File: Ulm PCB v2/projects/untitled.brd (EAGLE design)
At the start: 39.4 x 53.1 mm, 26 parts, among them U1 FT232RLSSOP, U2 MCP73831, U3 SPX3819-3.3, X2 USB-SMD-NS

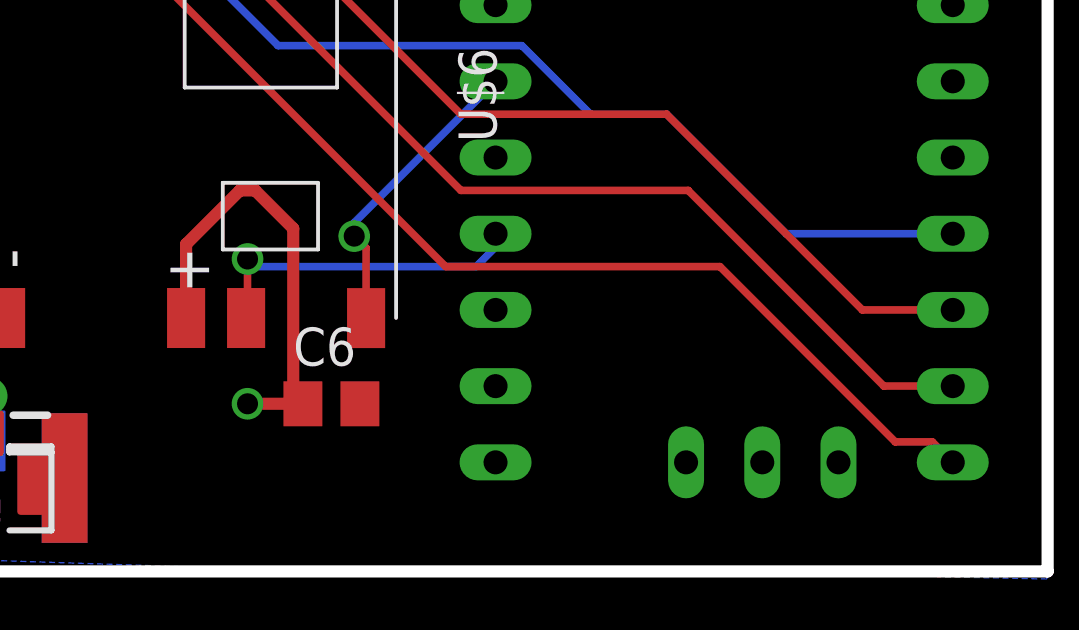
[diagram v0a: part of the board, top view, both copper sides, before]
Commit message: rerouted rmf power suppyl
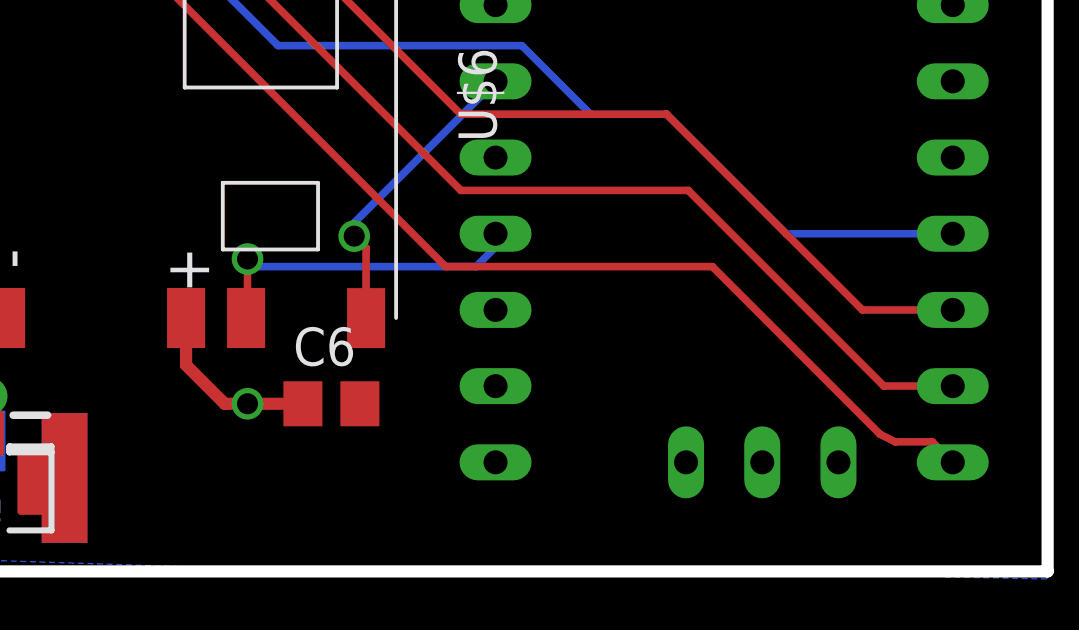
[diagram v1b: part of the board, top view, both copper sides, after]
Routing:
- net 3.3V: track 46.5 -> 37.9 mm
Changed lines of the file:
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@@
 <wire x1="0" y1="9.144" x2="39.37" y2="9.144" width="0.4064" layer="20"/>
 <wire x1="39.37" y1="9.144" x2="39.37" y2="62.23" width="0.4064" layer="20"/>
+<dimension x1="-0.508" y1="62.484" x2="-0.635" y2="9.144" x3="-7.555853125" y3="35.830628125" textsize="1.778" layer="1"/>
+<dimension x1="-0.508" y1="62.484" x2="39.4462" y2="62.4078" x3="19.482809375" y3="69.6344125" textsize="1.778" layer="1"/>
 </plain>
 <attributes>
@@
 <wire x1="27.178" y1="43.39936875" x2="27.3174625" y2="43.25990625" width="0.4064" layer="1"/>
 <wire x1="20.18615" y1="47.24329375" x2="20.828" y2="46.60144375" width="0.4064" layer="1"/>
-<wire x1="10.652" y1="17.5905" x2="10.652" y2="20.05" width="0.4064" layer="1"/>
-<wire x1="10.652" y1="20.05" x2="12.446" y2="21.844" width="0.4064" layer="1"/>
-<wire x1="12.446" y1="21.844" x2="12.954" y2="21.844" width="0.4064" layer="1"/>
-<wire x1="12.954" y1="21.844" x2="14.224" y2="20.574" width="0.4064" layer="1"/>
-<wire x1="14.224" y1="20.574" x2="14.224" y2="15.052" width="0.4064" layer="1"/>
 <wire x1="14.544" y1="14.732" x2="14.224" y2="15.052" width="0.4064" layer="1"/>
 <via x="12.7" y="14.732" extent="1-16" drill="0.7"/>
 <wire x1="12.7" y1="14.732" x2="14.544" y2="14.732" width="0.4064" layer="1"/>
 <wire x1="20.18615" y1="47.93765" x2="20.18615" y2="47.24329375" width="0.4064" layer="1"/>
+<wire x1="10.652" y1="17.5905" x2="10.652" y2="16.018" width="0.4064" layer="1"/>
+<wire x1="10.652" y1="16.018" x2="11.938" y2="14.732" width="0.4064" layer="1"/>
+<wire x1="11.938" y1="14.732" x2="12.7" y2="14.732" width="0.4064" layer="1"/>
 </signal>
 <signal name="TXLED">
@@
 <wire x1="8.652" y1="33.5905" x2="8.652" y2="29.956" width="0.254" layer="1"/>
 <wire x1="8.652" y1="29.956" x2="19.304" y2="19.304" width="0.254" layer="1"/>
-<wire x1="19.304" y1="19.304" x2="28.448" y2="19.304" width="0.254" layer="1"/>
-<wire x1="28.448" y1="19.304" x2="34.29" y2="13.462" width="0.254" layer="1"/>
 <wire x1="34.29" y1="13.462" x2="35.52536875" y2="13.462" width="0.254" layer="1"/>
 <wire x1="35.52536875" y1="13.462" x2="36.2074625" y2="12.77990625" width="0.254" layer="1"/>
+<wire x1="19.304" y1="19.304" x2="28.194" y2="19.304" width="0.254" layer="1"/>
+<wire x1="28.194" y1="19.304" x2="33.782" y2="13.716" width="0.254" layer="1"/>
+<wire x1="33.782" y1="13.716" x2="34.29" y2="13.462" width="0.254" layer="1"/>
 </signal>
 <signal name="LOL">

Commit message: rerouted arduino power suppyl
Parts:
- moved C7 2.54 mm to (28.4, 46.5)
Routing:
- net 3.3V: track 37.9 -> 34.0 mm
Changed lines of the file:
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@@
 </element>
 <element name="C6" library="rcl" package="C0805" value="100n" x="15.494" y="14.732"/>
-<element name="C7" library="rcl" package="C0805" value="100n" x="30.988" y="46.482"/>
+<element name="C7" library="rcl" package="C0805" value="100n" x="28.448" y="46.482"/>
 <element name="U$6" library="_c2h" package="RFM95" value="RFM95" x="9.652" y="23.368" rot="R270"/>
 <element name="C8" library="microbuilder" package="0805-NO" value="10µF" x="16.256" y="50.038" rot="R270"/>
@@
 </polygon>
 <wire x1="20.828" y1="46.60144375" x2="16.90025" y2="46.60144375" width="0.4064" layer="1"/>
-<wire x1="20.828" y1="46.60144375" x2="29.91855625" y2="46.60144375" width="0.4064" layer="1"/>
-<wire x1="29.91855625" y1="46.60144375" x2="30.038" y2="46.482" width="0.4064" layer="1"/>
-<wire x1="30.038" y1="46.482" x2="29.718" y2="46.482" width="0.4064" layer="1"/>
-<wire x1="29.718" y1="46.482" x2="27.178" y2="43.942" width="0.4064" layer="1"/>
-<wire x1="27.178" y1="43.942" x2="27.178" y2="43.39936875" width="0.4064" layer="1"/>
-<wire x1="27.178" y1="43.39936875" x2="27.3174625" y2="43.25990625" width="0.4064" layer="1"/>
 <wire x1="20.18615" y1="47.24329375" x2="20.828" y2="46.60144375" width="0.4064" layer="1"/>
 <wire x1="14.544" y1="14.732" x2="14.224" y2="15.052" width="0.4064" layer="1"/>
@@
 <wire x1="10.652" y1="16.018" x2="11.938" y2="14.732" width="0.4064" layer="1"/>
 <wire x1="11.938" y1="14.732" x2="12.7" y2="14.732" width="0.4064" layer="1"/>
+<wire x1="20.94744375" y1="46.482" x2="27.498" y2="46.482" width="0.4064" layer="1"/>
+<wire x1="20.94744375" y1="46.482" x2="20.828" y2="46.60144375" width="0.4064" layer="1"/>
+<wire x1="27.498" y1="46.482" x2="27.498" y2="43.44044375" width="0.4064" layer="1"/>
+<wire x1="27.498" y1="43.44044375" x2="27.3174625" y2="43.25990625" width="0.4064" layer="1"/>
+<wire x1="27.3174625" y1="43.25990625" x2="36.2074625" y2="33.09990625" width="0" layer="19" extent="1-1"/>
+<wire x1="20.828" y1="58.674" x2="20.18615" y2="47.93765" width="0" layer="19" extent="1-1"/>
+<wire x1="14.544" y1="14.732" x2="36.2074625" y2="33.09990625" width="0" layer="19" extent="1-1"/>
 </signal>
 <signal name="TXLED">

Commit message: nicing of batterycharger
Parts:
- moved C8 5.00 mm to (21.3, 50.0)
- moved D2 2.96 mm to (18.5, 51.8), turned to 90 degrees
- moved R2 0.30 mm to (19.3, 47.7)
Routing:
- net 5V: track 48.8 -> 48.1 mm
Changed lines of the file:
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@@
 <element name="LED2" library="SparkFun" package="LED-0603" value="Green" x="12.7" y="47.9552" rot="R90"/>
 <element name="R1" library="SparkFun" package="0402-RES" value="1K" x="16.25025" y="46.60144375"/>
-<element name="R2" library="SparkFun" package="0402-RES" value="1K" x="19.53615" y="47.93765"/>
+<element name="R2" library="SparkFun" package="0402-RES" value="1K" x="19.29815" y="47.74765"/>
 <element name="U$1" library="Arduino-clone" package="ABK-PRO-MINI" value="ABK-PRO-MINI" x="26.0474625" y="34.36990625"/>
 <element name="U1" library="SparkFun" package="SSOP28DB" value="FT232RLSSOP" x="9.144" y="40.386" rot="R90"/>
@@
 <element name="C7" library="rcl" package="C0805" value="100n" x="28.448" y="46.482"/>
 <element name="U$6" library="_c2h" package="RFM95" value="RFM95" x="9.652" y="23.368" rot="R270"/>
-<element name="C8" library="microbuilder" package="0805-NO" value="10µF" x="16.256" y="50.038" rot="R270"/>
+<element name="C8" library="microbuilder" package="0805-NO" value="10µF" x="21.256" y="50.038" rot="R270"/>
 <element name="C9" library="microbuilder" package="0603-NO" value="1uF" x="18.288" y="59.436" rot="R270"/>
 <element name="C10" library="microbuilder" package="0805-NO" value="10µF" x="16.51" y="59.436" rot="R270"/>
 <element name="U3" library="microbuilder" package="SOT23-5" value="SPX3819-3.3" x="13.462" y="57.658"/>
-<element name="D2" library="microbuilder" package="SOD-123" value="MBR120" x="16.002" y="53.34"/>
+<element name="D2" library="microbuilder" package="SOD-123" value="MBR120" x="18.542" y="51.816" rot="R90"/>
 <element name="R4" library="microbuilder" package="0603-NO" value="100k" x="17.018" y="56.388" rot="R180"/>
 <element name="J$2" library="_c2h" package="SMA_UFL_PAD_TINY" value="ANTENNATINY" x="4.064" y="9.906" rot="R270"/>
@@
 <via x="12.7" y="14.732" extent="1-16" drill="0.7"/>
 <wire x1="12.7" y1="14.732" x2="14.544" y2="14.732" width="0.4064" layer="1"/>
-<wire x1="20.18615" y1="47.93765" x2="20.18615" y2="47.24329375" width="0.4064" layer="1"/>
+<wire x1="19.94815" y1="47.74765" x2="20.18615" y2="47.24329375" width="0.4064" layer="1"/>
 <wire x1="10.652" y1="17.5905" x2="10.652" y2="16.018" width="0.4064" layer="1"/>
 <wire x1="10.652" y1="16.018" x2="11.938" y2="14.732" width="0.4064" layer="1"/>
@@
 <wire x1="27.498" y1="46.482" x2="27.498" y2="43.44044375" width="0.4064" layer="1"/>
 <wire x1="27.498" y1="43.44044375" x2="27.3174625" y2="43.25990625" width="0.4064" layer="1"/>
-<wire x1="27.3174625" y1="43.25990625" x2="36.2074625" y2="33.09990625" width="0" layer="19" extent="1-1"/>
-<wire x1="20.828" y1="58.674" x2="20.18615" y2="47.93765" width="0" layer="19" extent="1-1"/>
-<wire x1="14.544" y1="14.732" x2="36.2074625" y2="33.09990625" width="0" layer="19" extent="1-1"/>
 </signal>
 <signal name="TXLED">
@@
 <contactref element="LED2" pad="A"/>
 <wire x1="13.45" y1="47.9552" x2="18.8686" y2="47.9552" width="0.254" layer="1"/>
-<wire x1="18.8686" y1="47.9552" x2="18.88615" y2="47.93765" width="0.254" layer="1"/>
+<wire x1="18.8686" y1="47.9552" x2="18.64815" y2="47.74765" width="0.254" layer="1"/>
 </signal>
 <signal name="TXO">
@@
 <wire x1="12.512" y1="55.118" x2="12.512" y2="56.3579" width="0.4064" layer="1"/>
 <wire x1="12.512" y1="55.118" x2="12.512" y2="53.782" width="0.4064" layer="1"/>
-<wire x1="12.954" y1="53.34" x2="12.512" y2="53.782" width="0.4064" layer="1"/>
-<wire x1="12.954" y1="53.34" x2="14.152" y2="53.34" width="0.4064" layer="1"/>
-<wire x1="15.748" y1="50.7699" x2="24.45" y2="50.7699" width="0.4064" layer="1"/>
-<wire x1="15.748" y1="50.7699" x2="15.5241" y2="50.7699" width="0.4064" layer="1"/>
-<wire x1="15.5241" y1="50.7699" x2="12.954" y2="53.34" width="0.4064" layer="1"/>
-<wire x1="16.256" y1="50.988" x2="15.9661" y2="50.988" width="0.254" layer="1"/>
-<wire x1="15.9661" y1="50.988" x2="15.748" y2="50.7699" width="0.254" layer="1"/>
+<wire x1="18.796" y1="50.7699" x2="21.336" y2="50.7699" width="0.4064" layer="1"/>
+<wire x1="18.796" y1="50.7699" x2="15.5241" y2="50.7699" width="0.4064" layer="1"/>
+<wire x1="21.336" y1="50.7699" x2="24.45" y2="50.7699" width="0.4064" layer="1"/>
+<wire x1="15.5241" y1="50.7699" x2="12.512" y2="53.782" width="0.4064" layer="1"/>
 <wire x1="17.868" y1="56.388" x2="17.868" y2="55.46" width="0.254" layer="1"/>
 <wire x1="17.868" y1="55.46" x2="17.526" y2="55.118" width="0.254" layer="1"/>
@@
 <wire x1="7.874" y1="41.402" x2="5.529" y2="41.402" width="0.3048" layer="1"/>
 <wire x1="5.529" y1="41.402" x2="5.488" y2="41.361" width="0.3048" layer="1"/>
+<wire x1="21.256" y1="50.988" x2="21.256" y2="50.8499" width="0.4064" layer="1"/>
+<wire x1="21.256" y1="50.8499" x2="21.336" y2="50.7699" width="0.4064" layer="1"/>
+<wire x1="18.542" y1="49.966" x2="18.542" y2="50.5159" width="0.4064" layer="1"/>
+<wire x1="18.542" y1="50.5159" x2="18.796" y2="50.7699" width="0.4064" layer="1"/>
 </signal>
 <signal name="SCL">
@@
 <contactref element="U2" pad="3"/>
 <contactref element="J2" pad="2"/>
-<wire x1="17.8821" y1="53.3701" x2="24.45" y2="53.3701" width="0.4064" layer="1"/>
-<wire x1="17.8821" y1="53.3701" x2="17.852" y2="53.34" width="0.4064" layer="1"/>
+<wire x1="18.796" y1="53.3701" x2="17.8821" y2="53.3701" width="0.4064" layer="1"/>
+<wire x1="18.796" y1="53.3701" x2="24.45" y2="53.3701" width="0.4064" layer="1"/>
 <wire x1="24.45" y1="53.3701" x2="24.45" y2="54.842" width="0.4064" layer="1"/>
 <wire x1="24.45" y1="54.842" x2="24.638" y2="55.03" width="0.4064" layer="1"/>
 <wire x1="24.638" y1="55.03" x2="30.44" y2="55.03" width="0.4064" layer="1"/>
 <wire x1="30.44" y1="55.03" x2="30.59" y2="54.88" width="0.4064" layer="1"/>
+<wire x1="18.542" y1="53.666" x2="18.542" y2="53.6241" width="0.4064" layer="1"/>
+<wire x1="18.542" y1="53.6241" x2="18.796" y2="53.3701" width="0.4064" layer="1"/>
 </signal>
 <signal name="EN">

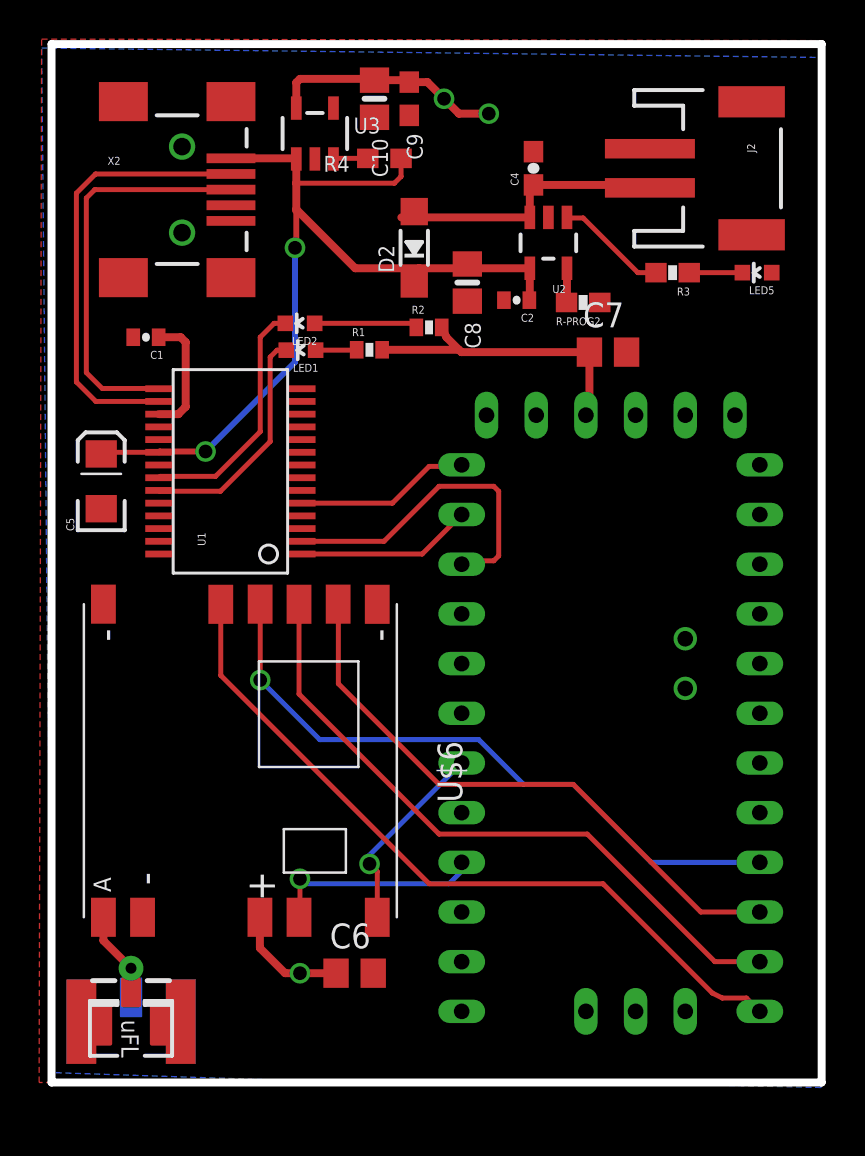
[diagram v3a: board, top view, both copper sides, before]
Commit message: WIP: reducing height. Antenna must be refitted
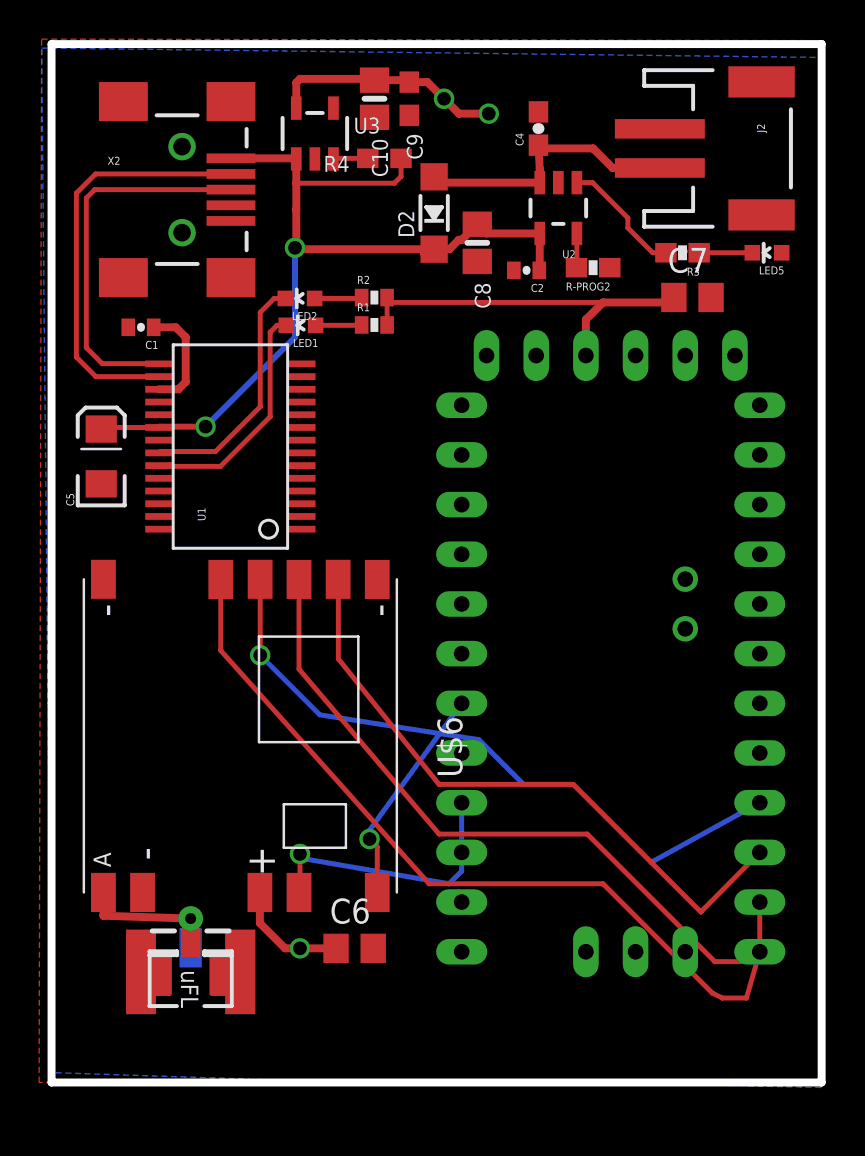
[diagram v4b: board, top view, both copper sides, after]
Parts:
- moved C7 5.14 mm to (32.8, 49.3)
- moved J$2 3.97 mm to (7.11, 12.4)
- moved R2 3.18 mm to (16.5, 49.3)
- moved U$1 3.05 mm to (26.0, 37.4)
- moved C8 2.09 mm to (21.8, 52.1)
- moved D2 2.05 mm to (19.6, 53.6)
- moved C4 2.05 mm to (24.9, 57.9)
- moved U2 1.85 mm to (25.9, 53.8)
- moved R-PROG2 1.85 mm to (27.7, 50.8)
- moved C2 1.61 mm to (24.3, 50.7)
- moved R1 1.30 mm to (16.5, 47.9)
- moved C5 1.27 mm to (2.54, 41.1)
- moved LED1 1.27 mm to (12.8, 47.9)
- moved LED2 1.27 mm to (12.7, 49.2)
- moved U$6 1.27 mm to (9.65, 24.6)
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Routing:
- net DTR: track 16.7 -> 0.00 mm
- net TXO: track 9.00 -> 0.00 mm
- net RXI: track 8.98 -> 0.00 mm
- net MOSI: track 33.8 -> 37.8 mm
- net 3.3V: track 33.8 -> 37.8 mm
- net N$2: track 5.72 -> 2.42 mm
- net D6: track 11.1 -> 14.2 mm
- net N$4: track 5.92 -> 8.38 mm
- net CS: track 38.3 -> 40.7 mm
- net MISO: track 30.5 -> 32.7 mm
- net D4: track 10.0 -> 11.4 mm
- net USB_D-: track 22.6 -> 21.3 mm
- net USB_D+: track 20.5 -> 19.3 mm
- net 5V: track 48.1 -> 46.9 mm
- net SCL: track 33.3 -> 34.2 mm
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
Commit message: Board now approx 5x4 cm
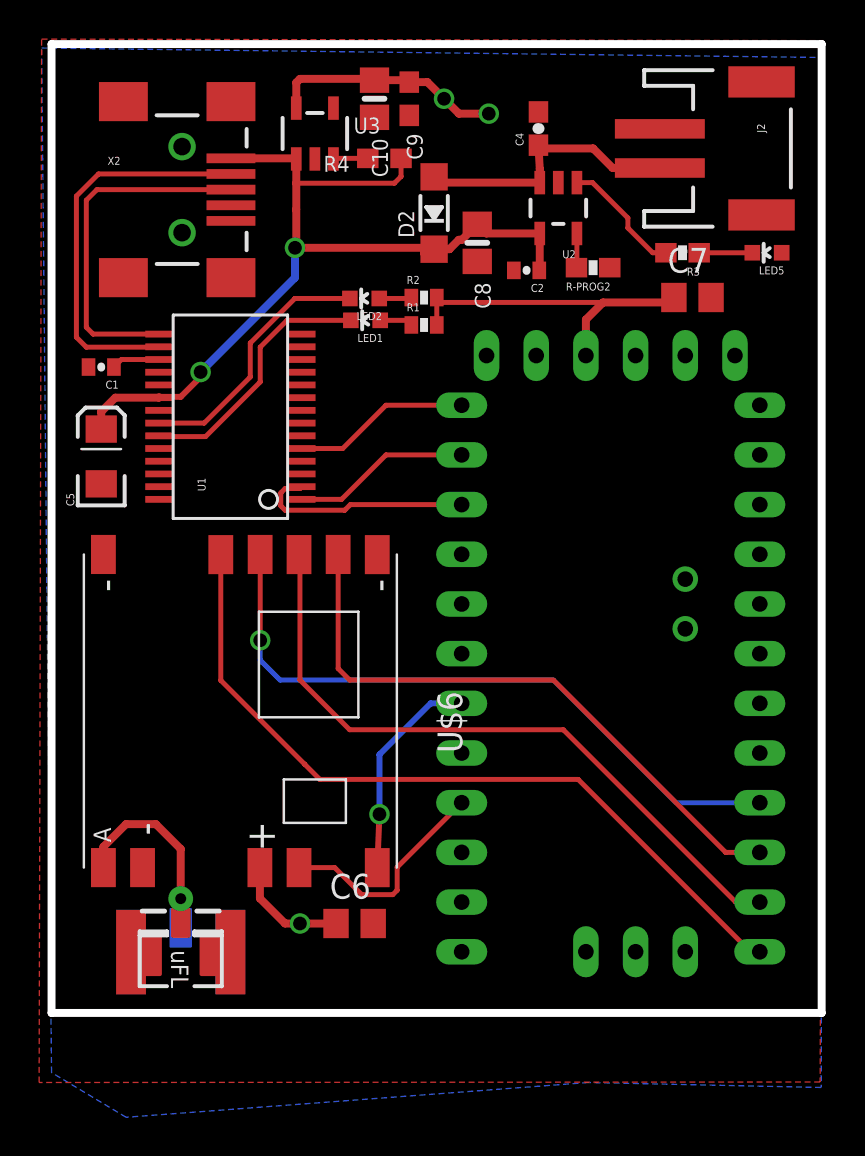
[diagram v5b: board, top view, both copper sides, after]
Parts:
- moved LED1 3.31 mm to (16.1, 48.1)
- moved LED2 3.30 mm to (16.0, 49.2)
- moved C1 2.87 mm to (2.54, 45.7)
- moved R1 2.54 mm to (19.0, 47.9)
- moved R2 2.54 mm to (19.0, 49.3)
- moved U1 1.52 mm to (9.14, 43.2)
- moved C6 1.27 mm to (15.5, 17.3)
- moved U$6 1.27 mm to (9.65, 25.9)
- moved J$2 1.14 mm to (6.60, 13.5)
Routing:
- net DTR: track 0.00 -> 11.3 mm
- net TXO: track 0.00 -> 9.11 mm
- net RXI: track 0.00 -> 9.08 mm
- net 123: track 5.66 -> 2.46 mm
- net MOSI: track 37.8 -> 34.6 mm
- net 3.3V: track 37.8 -> 34.8 mm
- net N$4: track 8.38 -> 11.3 mm
- net D6: track 14.2 -> 11.5 mm, vias 1 -> 0
- net MISO: track 32.7 -> 31.3 mm
- net USB_D+: track 19.3 -> 18.0 mm
- net USB_D-: track 21.3 -> 20.0 mm
- net TXLED: track 12.0 -> 13.3 mm
- net CS: track 40.7 -> 39.8 mm
- net 5V: track 46.9 -> 46.0 mm
- net RXLED: track 12.6 -> 13.4 mm
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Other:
- board size 39.4 x 53.1 mm -> 39.4 x 49.5 mm
